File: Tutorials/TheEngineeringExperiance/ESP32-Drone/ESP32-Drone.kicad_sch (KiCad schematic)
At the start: 0 parts

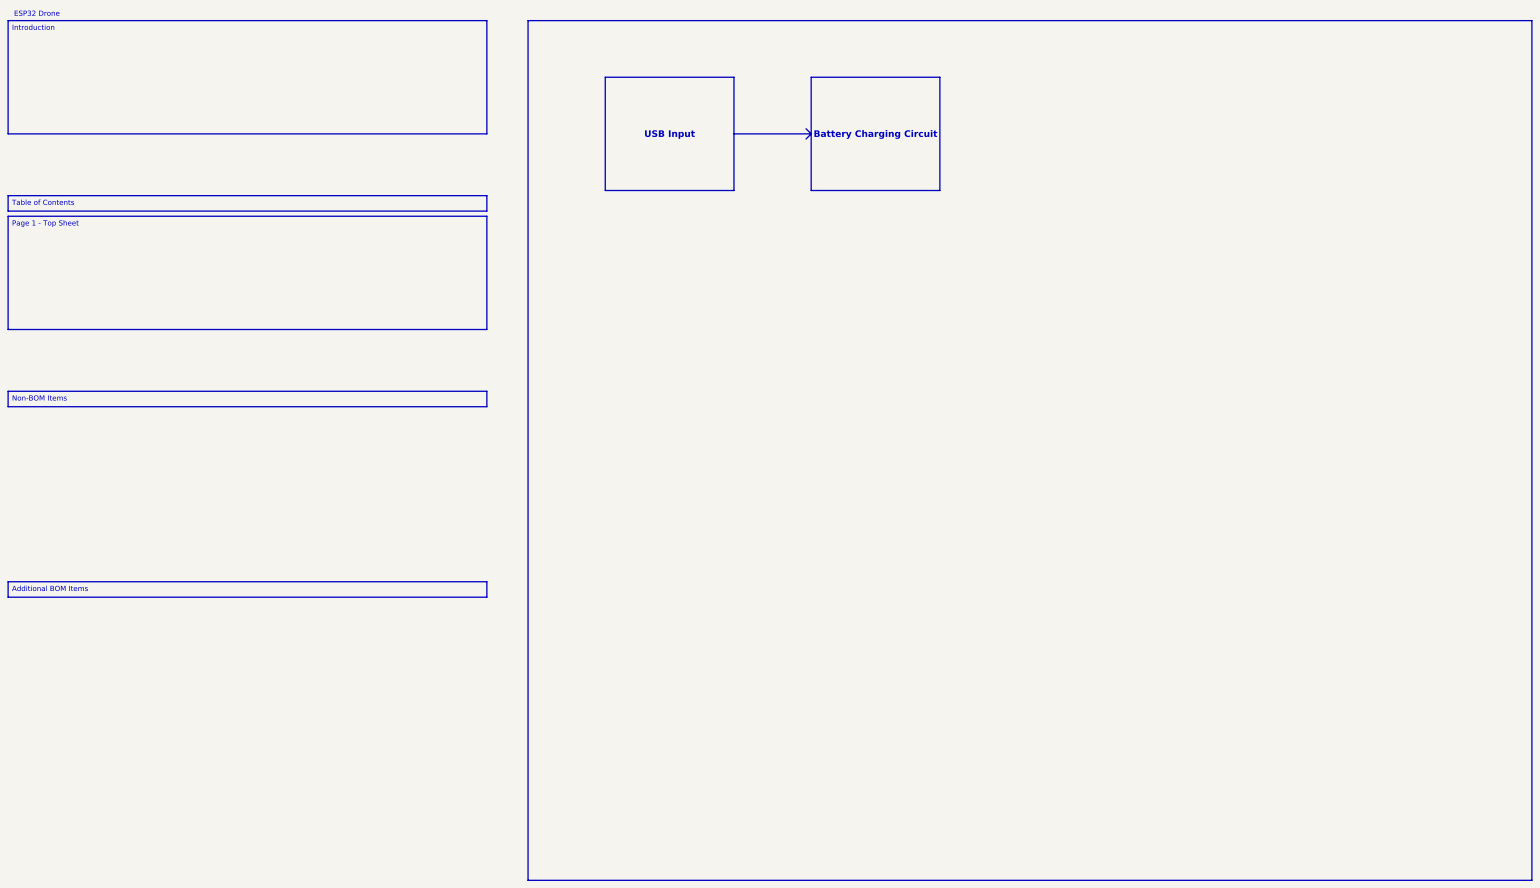
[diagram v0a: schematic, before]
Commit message: added 3 new sheets
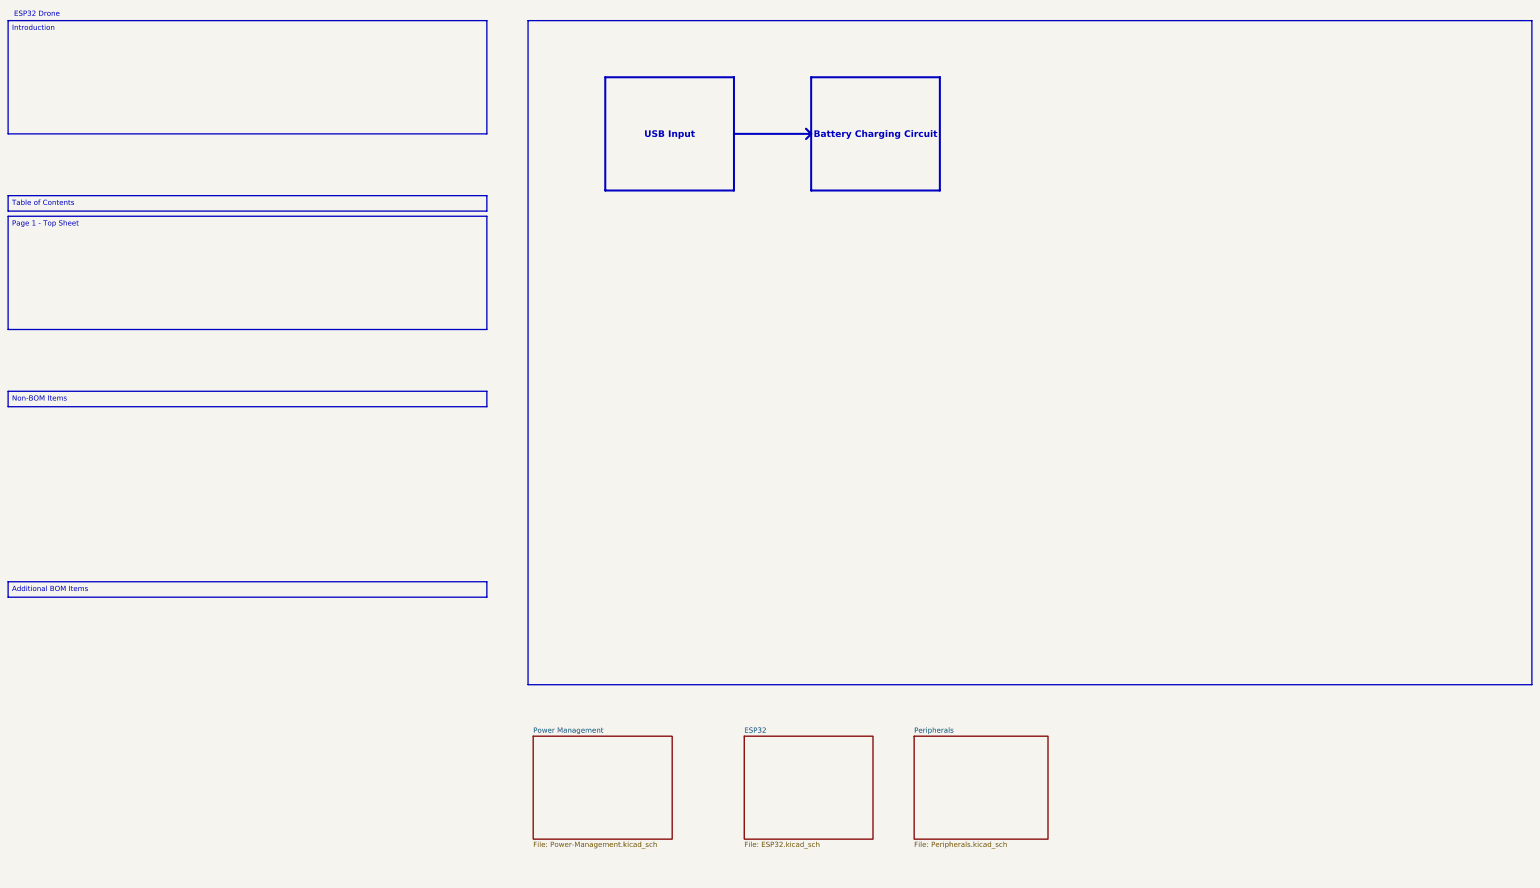
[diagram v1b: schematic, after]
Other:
- added sheet ESP32 (ESP32.kicad_sch)
- added sheet Peripherals (Peripherals.kicad_sch)
- added sheet Power Management (Power-Management.kicad_sch)
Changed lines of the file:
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@@
 	(rectangle
 		(start 152.4 22.86)
-		(end 400.05 234.95)
+		(end 400.05 186.69)
 		(stroke
 			(width 0)
@@
 		(margins 0.9525 0.9525 0.9525 0.9525)
 		(stroke
-			(width 0)
+			(width 0.5)
 			(type solid)
 		)
@@
 		(margins 0.9525 0.9525 0.9525 0.9525)
 		(stroke
-			(width 0)
+			(width 0.5)
 			(type solid)
 		)
@@
 		)
 		(stroke
+			(width 0.5)
+			(type solid)
+		)
+	)
+	(polyline
+		(pts
+			(xy 220.98 49.53) (xy 222.25 50.8)
+		)
+		(stroke
 			(width 0)
 			(type default)
@@
 		)
 		(stroke
-			(width 0)
+			(width 0.5)
 			(type default)
 		)
@@
 		)
 		(stroke
-			(width 0)
-			(type default)
-		)
-	)
+			(width 0.5)
+			(type default)
+		)
+	)
+	(polyline
+		(pts
+			(xy 220.98 49.53) (xy 222.25 50.8)
+		)
+		(stroke
+			(width 0)
+			(type default)
+		)
+	)
+	(sheet
+		(at 247.65 199.39)
+		(size 33.02 25.4)
+		(exclude_from_sim no)
+		(in_bom yes)
+		(on_board yes)
+		(dnp no)
+		(fields_autoplaced yes)
+		(stroke
+			(width 0.1524)
+			(type solid)
+		)
+		(fill
+			(color 0 0 0 0.0000)
+		)
+		(property "Sheetname" "Peripherals"
+			(at 247.65 198.6784 0)
+			(effects
+				(font
+					(size 1.27 1.27)
+				)
+				(justify left bottom)
+			)
+		)
+		(property "Sheetfile" "Peripherals.kicad_sch"
+			(at 247.65 225.3746 0)
+			(effects
+				(font
+					(size 1.27 1.27)
+				)
+				(justify left top)
+			)
+		)
+		(instances
+			(project "ESP32-Drone"
+				(path "/2164f6c4-476c-4035-8d45-cddfb758dbad"
+					(page "4")
+				)
+			)
+		)
+	)
+	(sheet
+		(at 153.67 199.39)
+		(size 34.29 25.4)
+		(exclude_from_sim no)
+		(in_bom yes)
+		(on_board yes)
+		(dnp no)
+		(fields_autoplaced yes)
+		(stroke
+			(width 0.1524)
+			(type solid)
+		)
+		(fill
+			(color 0 0 0 0.0000)
+		)
+		(property "Sheetname" "Power Management"
+			(at 153.67 198.6784 0)
+			(effects
+				(font
+					(size 1.27 1.27)
+				)
+				(justify left bottom)
+			)
+		)
+		(property "Sheetfile" "Power-Management.kicad_sch"
+			(at 153.67 225.3746 0)
+			(effects
+				(font
+					(size 1.27 1.27)
+				)
+				(justify left top)
+			)
+		)
+		(instances
+			(project "ESP32-Drone"
+				(path "/2164f6c4-476c-4035-8d45-cddfb758dbad"
+					(page "2")
+				)
+			)
+		)
+	)
+	(sheet
+		(at 205.74 199.39)
+		(size 31.75 25.4)
+		(exclude_from_sim no)
+		(in_bom yes)
+		(on_board yes)
+		(dnp no)
+		(fields_autoplaced yes)
+		(stroke
+			(width 0.1524)
+			(type solid)
+		)
+		(fill
+			(color 0 0 0 0.0000)
+		)
+		(property "Sheetname" "ESP32"
+			(at 205.74 198.6784 0)
+			(effects
+				(font
+					(size 1.27 1.27)
+				)
+				(justify left bottom)
+			)
+		)
+		(property "Sheetfile" "ESP32.kicad_sch"
+			(at 205.74 225.3746 0)
+			(effects
+				(font
+					(size 1.27 1.27)
+				)
+				(justify left top)
+			)
+		)
+		(instances
+			(project "ESP32-Drone"
+				(path "/2164f6c4-476c-4035-8d45-cddfb758dbad"
+					(page "3")
+				)
+			)
+		)
+	)

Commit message: added title
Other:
- note added: "System Diagram (Block Diagram)"
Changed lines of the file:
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@@
+		)
+	)
+	(text "System Diagram (Block Diagram)"
+		(exclude_from_sim no)
+		(at 188.468 38.354 0)
+		(effects
+			(font
+				(size 2 2)
+				(thickness 0.4)
+				(bold yes)
+			)
 		)
 	)
 	(text_box "USB Input"
 		(exclude_from_sim no)
-		(at 171.45 36.83 0)
+		(at 172.72 54.61 0)
 		(size 31.75 27.94)
 		(margins 0.9525 0.9525 0.9525 0.9525)
@@
 	(text_box "Battery Charging Circuit"
 		(exclude_from_sim no)
-		(at 222.25 36.83 0)
+		(at 223.52 54.61 0)
 		(size 31.75 27.94)
 		(margins 0.9525 0.9525 0.9525 0.9525)
@@
 	(polyline
 		(pts
-			(xy 203.2 50.8) (xy 222.25 50.8)
+			(xy 204.47 68.58) (xy 223.52 68.58)
 		)
 		(stroke
@@
 	(polyline
 		(pts
-			(xy 220.98 49.53) (xy 222.25 50.8)
+			(xy 222.25 67.31) (xy 223.52 68.58)
 		)
 		(stroke
@@
 	(polyline
 		(pts
-			(xy 220.98 52.07) (xy 222.25 50.8)
+			(xy 222.25 69.85) (xy 223.52 68.58)
 		)
 		(stroke
@@
 	(polyline
 		(pts
-			(xy 220.98 49.53) (xy 222.25 50.8)
+			(xy 222.25 67.31) (xy 223.52 68.58)
 		)
 		(stroke
@@
 	(polyline
 		(pts
-			(xy 220.98 49.53) (xy 222.25 50.8)
+			(xy 222.25 67.31) (xy 223.52 68.58)
 		)
 		(stroke
